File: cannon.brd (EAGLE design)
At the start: 82.5 x 82.5 mm, 55 parts, among them J1 RJ45

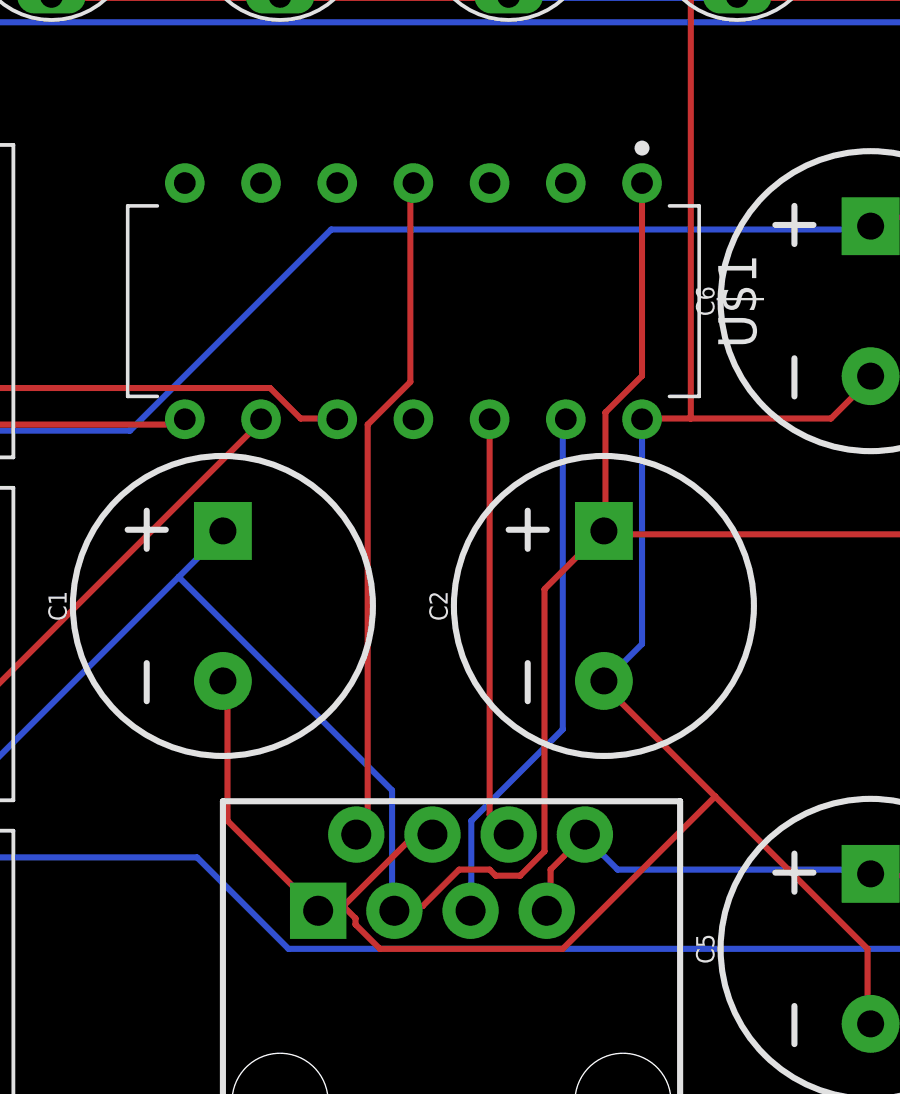
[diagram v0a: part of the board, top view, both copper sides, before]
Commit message: Updated Board, Removed In Circuit programming
Adjusted RJ45 pins for POE standard BOARD DESIGN NOT CHANGED!!! DO NOT USE TO MAKE BOARDS
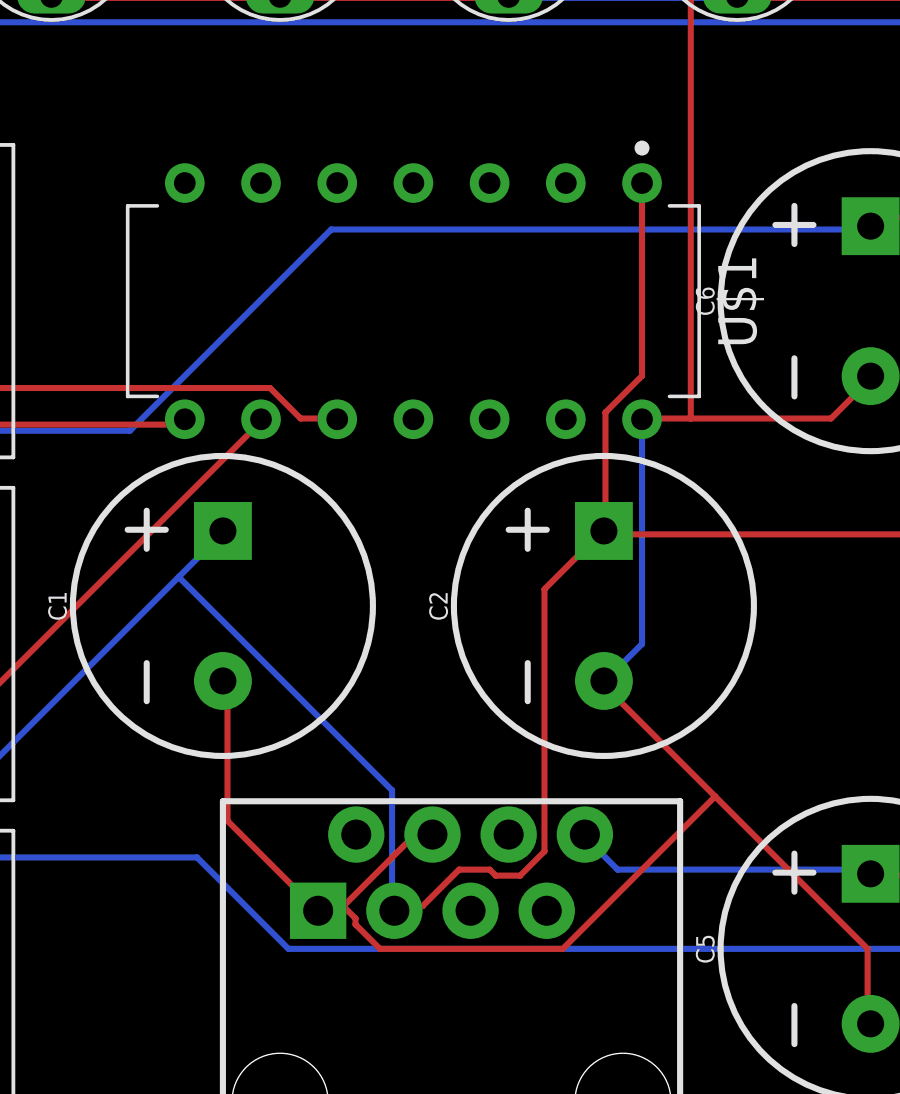
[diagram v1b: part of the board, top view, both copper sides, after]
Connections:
- removed net N$23: J1.5, U$1.13
- removed net N$24: J1.6, U$1.12
- removed net N$8: J1.2, U$1.4
- new net N$1: J1.1, U$1.12
- new net N$2: J1.3, U$1.13
- net GND: now also J1.7, J1.8; no longer J1.1, J1.4
- net N$25: now also J1.4, J1.5; no longer J1.7, J1.8
- net VCC_RED: no longer J1.3
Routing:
- net N$8: track 22.6 -> 0.00 mm
- net N$23: track 17.7 -> 0.00 mm
- net N$24: track 14.1 -> 0.00 mm
- net N$25: track 113.5 -> 110.2 mm
- net GND: track 354.3 -> 352.8 mm
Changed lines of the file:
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@@
 <?xml version="1.0" encoding="utf-8"?>
 <!DOCTYPE eagle SYSTEM "eagle.dtd">
-<eagle version="9.3.0">
+<eagle version="9.3.2">
 <drawing>
 <settings>
@@
 <contactref element="U$1" pad="1"/>
 <contactref element="C1" pad="+"/>
-<contactref element="J1" pad="3"/>
 <contactref element="C2" pad="+"/>
 <contactref element="RED+PIC" pad="OUT"/>
@@
 <wire x1="37.3888" y1="15.4432" x2="37.3888" y2="11.5824" width="0.2032" layer="16"/>
 <wire x1="30.2768" y1="22.5552" x2="37.3888" y2="15.4432" width="0.2032" layer="16"/>
-<wire x1="37.3888" y1="11.5824" x2="37.465" y2="11.43" width="0.2032" layer="16"/>
 <wire x1="45.72" y1="29.2608" x2="45.72" y2="35.687" width="0.2032" layer="1"/>
 <wire x1="44.5008" y1="28.0416" x2="45.72" y2="29.2608" width="0.2032" layer="1"/>
@@
 <wire x1="42.4688" y1="22.1488" x2="42.4688" y2="13.4112" width="0.2032" layer="1"/>
 <wire x1="44.2976" y1="23.9776" x2="42.4688" y2="22.1488" width="0.2032" layer="1"/>
-<wire x1="37.592" y1="11.5824" x2="37.465" y2="11.43" width="0.2032" layer="1"/>
 <wire x1="44.2976" y1="23.9776" x2="44.45" y2="24.09" width="0.2032" layer="1"/>
+<wire x1="37.3888" y1="11.5824" x2="37.592" y2="11.5824" width="0" layer="19" extent="1-16"/>
 </signal>
 <signal name="N$5">
@@
 <wire x1="48.9712" y1="53.4416" x2="48.895" y2="53.34" width="0.2032" layer="1"/>
 </signal>
-<signal name="N$23">
-<contactref element="U$1" pad="13"/>
-<contactref element="J1" pad="5"/>
-<wire x1="43.0784" y1="17.4752" x2="43.0784" y2="27.6352" width="0.2032" layer="16"/>
-<wire x1="40.0304" y1="14.4272" x2="43.0784" y2="17.4752" width="0.2032" layer="16"/>
-<wire x1="40.0304" y1="11.5824" x2="40.0304" y2="14.4272" width="0.2032" layer="16"/>
-<wire x1="43.0784" y1="27.6352" x2="43.18" y2="27.813" width="0.2032" layer="16"/>
-<wire x1="40.0304" y1="11.5824" x2="40.005" y2="11.43" width="0.2032" layer="16"/>
-</signal>
-<signal name="N$24">
-<contactref element="U$1" pad="12"/>
-<contactref element="J1" pad="6"/>
-<wire x1="40.64" y1="14.6304" x2="40.64" y2="27.813" width="0.2032" layer="1"/>
-<wire x1="41.2496" y1="14.0208" x2="40.64" y2="14.6304" width="0.2032" layer="1"/>
-<wire x1="41.2496" y1="14.0208" x2="41.275" y2="13.97" width="0.2032" layer="1"/>
-</signal>
-<signal name="N$8">
-<contactref element="J1" pad="2"/>
-<contactref element="U$1" pad="4"/>
-<wire x1="37.9984" y1="29.0576" x2="37.9984" y2="35.56" width="0.2032" layer="1"/>
-<wire x1="36.576" y1="27.6352" x2="37.9984" y2="29.0576" width="0.2032" layer="1"/>
-<wire x1="36.576" y1="14.224" x2="36.576" y2="27.6352" width="0.2032" layer="1"/>
-<wire x1="36.3728" y1="14.0208" x2="36.576" y2="14.224" width="0.2032" layer="1"/>
-<wire x1="37.9984" y1="35.56" x2="38.1" y2="35.687" width="0.2032" layer="1"/>
-<wire x1="36.3728" y1="14.0208" x2="36.195" y2="13.97" width="0.2032" layer="1"/>
-</signal>
 <signal name="VCC_BLUE">
 <contactref element="BLUE" pad="OUT"/>
@@
 <contactref element="C5" pad="+"/>
 <contactref element="GREEN" pad="IN"/>
-<contactref element="J1" pad="8"/>
-<contactref element="J1" pad="7"/>
 <contactref element="C3" pad="+"/>
 <contactref element="RED+PIC" pad="IN"/>
 <contactref element="BLUE" pad="IN"/>
 <contactref element="C7" pad="+"/>
-<wire x1="42.672" y1="12.8016" x2="42.672" y2="11.5824" width="0.2032" layer="1"/>
-<wire x1="43.688" y1="13.8176" x2="42.672" y2="12.8016" width="0.2032" layer="1"/>
-<wire x1="42.672" y1="11.5824" x2="42.545" y2="11.43" width="0.2032" layer="1"/>
-<wire x1="43.688" y1="13.8176" x2="43.815" y2="13.97" width="0.2032" layer="1"/>
 <wire x1="44.9072" y1="12.8016" x2="53.2384" y2="12.8016" width="0.2032" layer="16"/>
 <wire x1="43.8912" y1="13.8176" x2="44.9072" y2="12.8016" width="0.2032" layer="16"/>
 <wire x1="53.2384" y1="12.8016" x2="53.34" y2="12.66" width="0.2032" layer="16"/>
-<wire x1="43.8912" y1="13.8176" x2="43.815" y2="13.97" width="0.2032" layer="16"/>
 <wire x1="80.6704" y1="8.3312" x2="78.8416" y2="6.5024" width="0.2032" layer="1"/>
 <wire x1="80.6704" y1="15.8496" x2="80.6704" y2="8.3312" width="0.2032" layer="1"/>
@@
 <wire x1="53.4416" y1="12.5984" x2="53.34" y2="12.66" width="0.2032" layer="1"/>
 <wire x1="78.6384" y1="6.5024" x2="78.74" y2="6.35" width="0.2032" layer="1"/>
+<contactref element="J1" pad="5"/>
+<contactref element="J1" pad="4"/>
+<wire x1="40.005" y1="11.43" x2="43.8912" y2="13.8176" width="0" layer="19" extent="16-16"/>
+<wire x1="38.735" y1="13.97" x2="40.005" y2="11.43" width="0" layer="19" extent="1-1"/>
 </signal>
 <signal name="GND">
@@
 <contactref element="U$1" pad="14"/>
 <contactref element="C1" pad="-"/>
-<contactref element="J1" pad="1"/>
-<contactref element="J1" pad="4"/>
 <contactref element="C3" pad="-"/>
 <contactref element="C2" pad="-"/>
@@
 <wire x1="37.9984" y1="13.8176" x2="35.7632" y2="11.5824" width="0.2032" layer="1"/>
 <wire x1="38.608" y1="13.8176" x2="37.9984" y2="13.8176" width="0.2032" layer="1"/>
-<wire x1="34.9504" y1="11.5824" x2="34.925" y2="11.43" width="0.2032" layer="1"/>
-<wire x1="38.608" y1="13.8176" x2="38.735" y2="13.97" width="0.2032" layer="1"/>
 <wire x1="31.9024" y1="14.4272" x2="31.9024" y2="18.8976" width="0.2032" layer="1"/>
 <wire x1="34.7472" y1="11.5824" x2="31.9024" y2="14.4272" width="0.2032" layer="1"/>
 <wire x1="31.9024" y1="18.8976" x2="31.75" y2="19.09" width="0.2032" layer="1"/>
-<wire x1="34.7472" y1="11.5824" x2="34.925" y2="11.43" width="0.2032" layer="1"/>
 <wire x1="52.0192" y1="27.8384" x2="47.3456" y2="27.8384" width="0.2032" layer="1"/>
 <wire x1="47.3456" y1="27.8384" x2="45.72" y2="27.8384" width="0.2032" layer="1"/>
@@
 <wire x1="43.0784" y1="10.16" x2="36.9824" y2="10.16" width="0.2032" layer="1"/>
 <wire x1="48.1584" y1="15.24" x2="43.0784" y2="10.16" width="0.2032" layer="1"/>
-<wire x1="35.7632" y1="11.5824" x2="34.925" y2="11.43" width="0.2032" layer="1"/>
 <wire x1="33.528" y1="44.5008" x2="27.432" y2="44.5008" width="0.2032" layer="1"/>
 <wire x1="27.432" y1="44.5008" x2="26.2128" y2="44.5008" width="0.2032" layer="1"/>
@@
 <wire x1="56.6928" y1="44.2976" x2="57.3024" y2="44.2976" width="0.2032" layer="1"/>
 <wire x1="56.6928" y1="44.2976" x2="56.515" y2="44.45" width="0.2032" layer="1"/>
+<contactref element="J1" pad="8"/>
+<contactref element="J1" pad="7"/>
+<wire x1="42.545" y1="11.43" x2="43.815" y2="13.97" width="0" layer="19" extent="1-1"/>
+<wire x1="43.0784" y1="10.16" x2="42.545" y2="11.43" width="0" layer="19" extent="1-1"/>
+<wire x1="34.7472" y1="11.5824" x2="34.9504" y2="11.5824" width="0" layer="19" extent="1-1"/>
 </signal>
 <signal name="N$4">
@@
 <wire x1="33.655" y1="45.72" x2="41.275" y2="45.72" width="0.2032" layer="1"/>
 </signal>
+<signal name="N$1">
+<contactref element="U$1" pad="12"/>
+<contactref element="J1" pad="1"/>
+<wire x1="34.925" y1="11.43" x2="40.64" y2="27.813" width="0" layer="19" extent="1-1"/>
+</signal>
+<signal name="N$2">
+<contactref element="U$1" pad="13"/>
+<contactref element="J1" pad="3"/>
+<wire x1="37.465" y1="11.43" x2="43.18" y2="27.813" width="0" layer="19" extent="1-1"/>
+</signal>
 </signals>

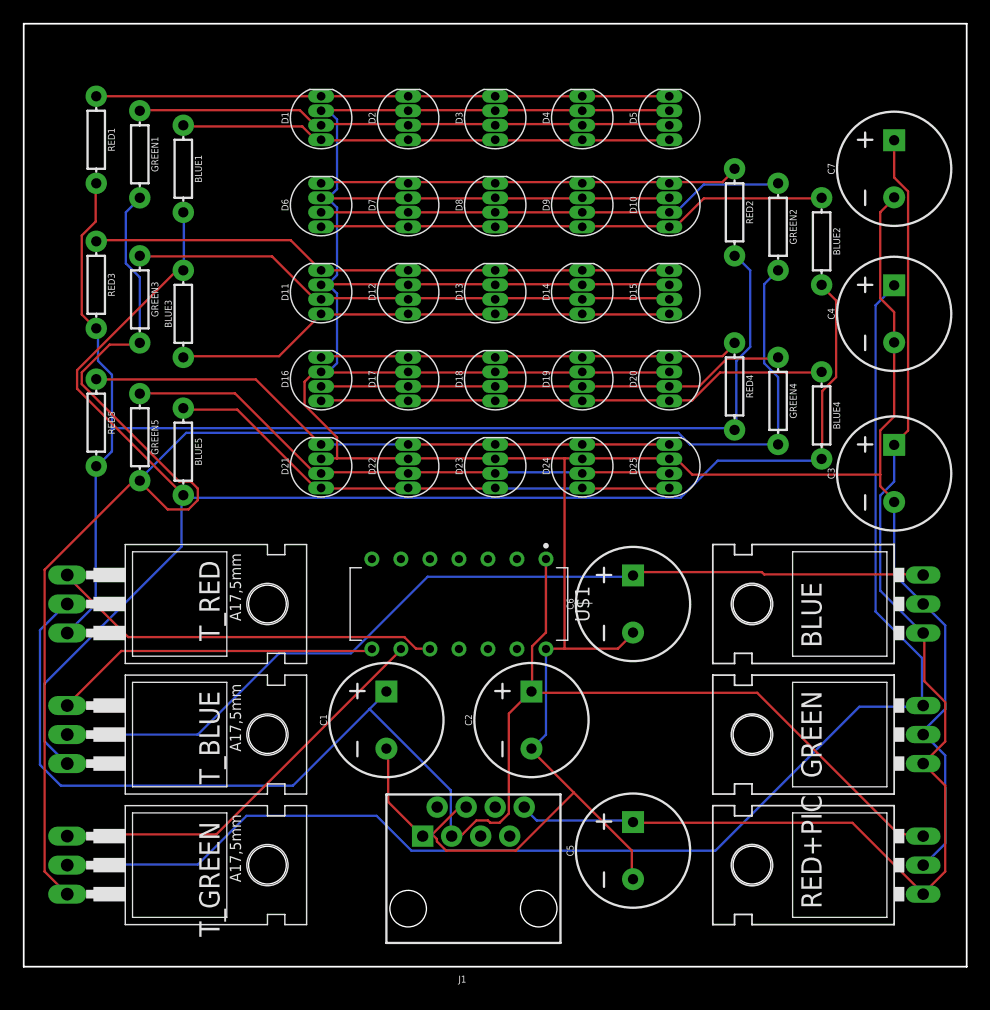
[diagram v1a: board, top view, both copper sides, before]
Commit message: Updated everything
Updated capacitor size, transistor pad, power reg pad, and LED pad
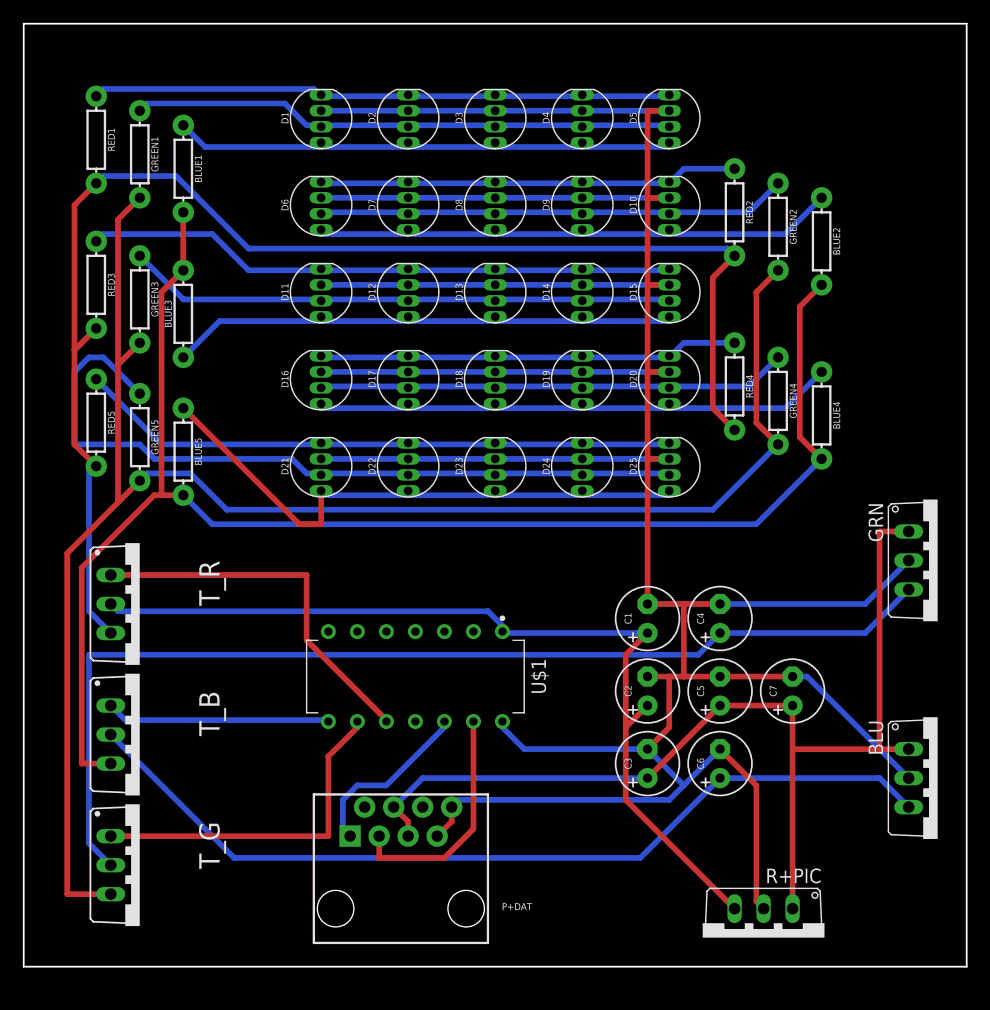
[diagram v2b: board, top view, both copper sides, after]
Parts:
- removed BLUE, GREEN, RED+PIC: (no value), SparkFun-IC-Power:TO-220-ALT
- removed J1: RJ45, SparkFun-Connectors:RJ45-8
- removed T_BLUE, T_GREEN, T_RED: 2N5496, transistor:TO220
- added BLU, GRN, R+PIC: (no value), linear:TO220V
- added P+DAT: RJ45, SparkFun-Connectors:RJ45-8
- added T_B, T_G, T_R: BD241C, transistor:TO220BV
- C1, C2, C3, C4, C5, C6, C7: device SparkFun-Capacitors:CPOL-RADIAL-5MM-10MM -> BeagleBone_Blue_R3:E2,5-6
- D1, D10, D11, D12, D13, D14, D15, D16, D17, D18, D19, D2, D20, D21, D22, D23, D24, D25, D3, D4, D5, D6, D7, D8, D9: device SparkFun-LED:LED-RGB-THRU -> SparkFun-LED_MOD:LED-RGB-THRU
- moved C7 46.6 mm to (67.3, 24.1)
- moved C3 33.3 mm to (54.6, 17.8)
- moved C4 30.7 mm to (61.0, 30.5)
- moved C1 24.5 mm to (54.6, 30.5)
- moved C5 15.9 mm to (61.0, 24.1)
- moved C6 15.9 mm to (61.0, 17.8)
- moved C2 10.5 mm to (54.6, 24.1)
- moved U$1 7.41 mm to (34.3, 25.4)
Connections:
- net GND: now also BLU.2, GRN.2, P+DAT.7, P+DAT.8, R+PIC.2; no longer BLUE.GND, GREEN.GND, J1.7, J1.8, RED+PIC.GND
- net N$1: now also P+DAT.1; no longer J1.1
- net N$17: now also T_B.3; no longer T_BLUE.3
- net N$2: now also P+DAT.3; no longer J1.3
- net N$22: now also T_G.3; no longer T_GREEN.3
- net N$25: now also BLU.1, GRN.1, P+DAT.4, P+DAT.5, R+PIC.1; no longer BLUE.IN, GREEN.IN, J1.4, J1.5, RED+PIC.IN
- net N$4: now also T_R.3; no longer T_RED.3
- net N$5: now also T_R.1; no longer T_RED.1
- net N$6: now also T_G.1; no longer T_GREEN.1
- net N$7: now also T_B.1; no longer T_BLUE.1
- net T_BLUE: now also GRN.3, T_G.2; no longer GREEN.OUT, T_GREEN.2
- net VCC_BLUE: now also BLU.3, T_B.2; no longer BLUE.OUT, T_BLUE.2
- net VCC_RED: now also R+PIC.3, T_R.2; no longer RED+PIC.OUT, T_RED.2
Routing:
- net VCC_RED: track 132.6 -> 80.0 mm
- net T_BLUE: track 122.4 -> 93.3 mm
- net N$2: track 0.00 -> 20.6 mm
- net GND: track 352.8 -> 332.3 mm
- net N$25: track 110.2 -> 91.2 mm
- net N$26: track 49.7 -> 67.7 mm
- net N$1: track 0.00 -> 15.8 mm
- net N$7: track 28.8 -> 19.7 mm
- net N$22: track 157.5 -> 149.4 mm
- net N$4: track 113.8 -> 120.9 mm
- net N$6: track 36.1 -> 30.1 mm
- net N$27: track 45.7 -> 51.6 mm
- net N$17: track 136.3 -> 132.9 mm
- net VCC_BLUE: track 80.9 -> 78.3 mm
- net N$20: track 45.0 -> 47.0 mm
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
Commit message: Modified traces and holes
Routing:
- net N$2: track 20.6 -> 24.2 mm
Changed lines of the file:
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@@
 <?xml version="1.0" encoding="utf-8"?>
 <!DOCTYPE eagle SYSTEM "eagle.dtd">
-<eagle version="9.3.2">
+<eagle version="9.2.2">
 <drawing>
 <settings>
@@
 <wire x1="82.55" y1="82.55" x2="82.55" y2="0" width="0.1524" layer="20"/>
 <wire x1="82.55" y1="0" x2="0" y2="0" width="0.1524" layer="20"/>
+<hole x="3.81" y="78.74" drill="1"/>
+<hole x="78.74" y="78.74" drill="1"/>
+<hole x="19.05" y="5.08" drill="1"/>
+<hole x="77.47" y="5.08" drill="1"/>
 </plain>
 <attributes>
@@
 <contactref element="P+DAT" pad="3"/>
 <wire x1="39.37" y1="12.065" x2="39.37" y2="21.463" width="0.5" layer="1"/>
-<wire x1="36.83" y1="9.525" x2="39.37" y2="12.065" width="0.5" layer="1"/>
-<wire x1="31.115" y1="9.525" x2="36.83" y2="9.525" width="0.5" layer="1"/>
-<wire x1="31.115" y1="11.43" x2="31.115" y2="9.525" width="0.5" layer="1"/>
+<wire x1="34.29" y1="6.985" x2="39.37" y2="12.065" width="0.5" layer="1"/>
+<wire x1="31.115" y1="6.985" x2="34.29" y2="6.985" width="0.5" layer="1"/>
+<wire x1="31.115" y1="11.43" x2="31.115" y2="6.985" width="0.5" layer="1"/>
 </signal>
 </signals>
